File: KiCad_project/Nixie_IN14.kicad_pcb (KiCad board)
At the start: 2 copper layers, 455.7 x 86.7 mm, 62 parts, among them J1 Conn_01x10_Pin, J2 Conn_01x07_Pin, J3 Conn_01x07_Pin, J4 Conn_01x10_Pin, J5 Conn_01x07_Pin, J6 Conn_01x07_Pin, J7 USB_C_Receptacle_PowerOnly_6P, Q1 IRF540N, Q2 MMBTA42, U1 BME280_module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

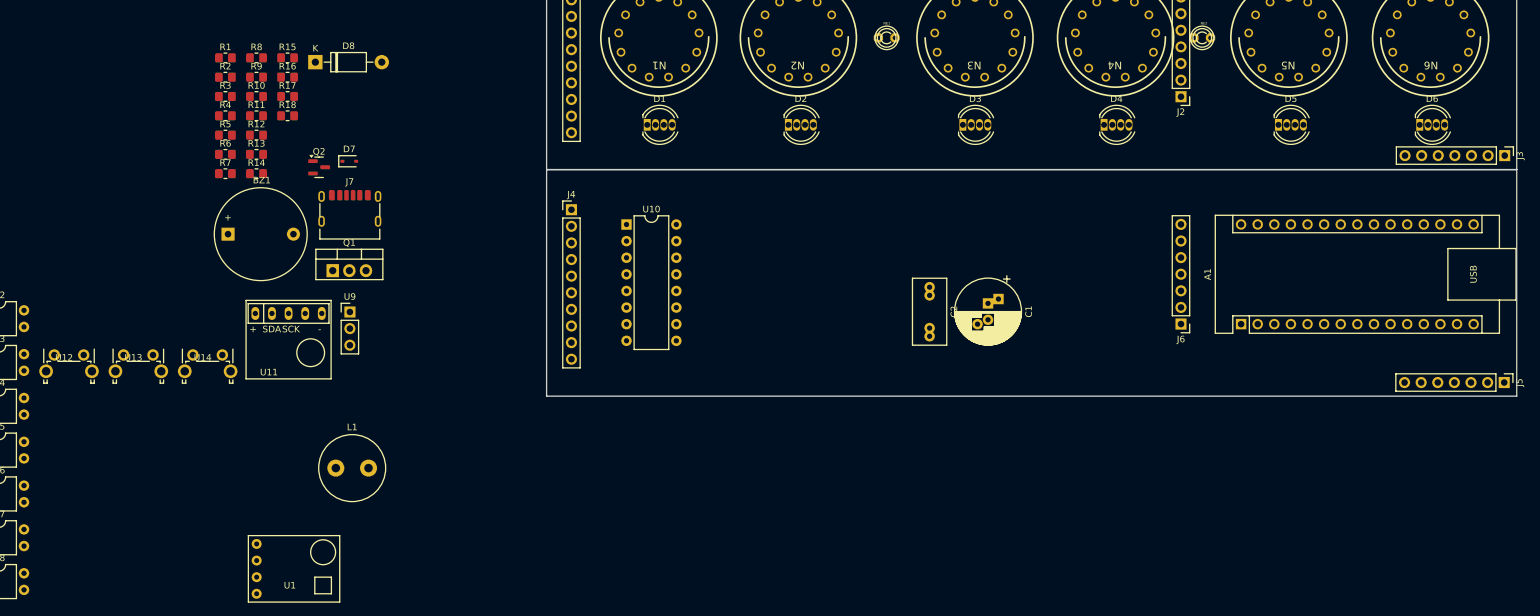
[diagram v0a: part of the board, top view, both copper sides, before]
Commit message: added missed power capacitors fixed some resistor values continue placing elements on the PCB
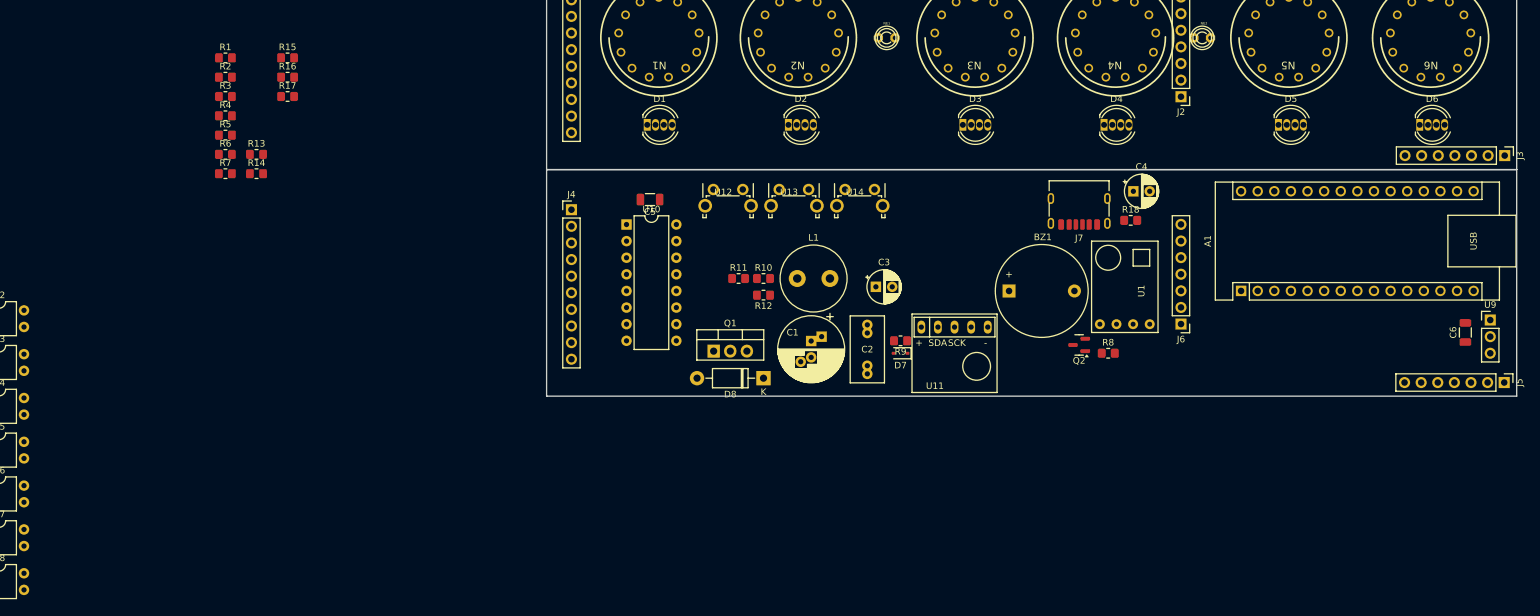
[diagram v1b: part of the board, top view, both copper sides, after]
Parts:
- added C3: 470uF x 6.3V, Capacitor_THT:CP_Radial_D5.0mm_P2.50mm, F.Cu at (194.3, -51.4)
- added C4: 470uF x 6.3V, Capacitor_THT:CP_Radial_D5.0mm_P2.50mm, F.Cu at (233.7, -66.0)
- added C5: 0.1uF, Capacitor_SMD:C_1206_3216Metric, F.Cu at (159.8, -64.8)
- added C6: 0.1uF, Capacitor_SMD:C_1206_3216Metric, F.Cu at (284.5, -44.5)
- moved U9 174.4 mm to (288.3, -46.4)
- moved R8 137.8 mm to (229.9, -41.3)
- moved U1 132.6 mm to (227.3, -44.5), turned to 90 degrees
- moved R18 129.9 mm to (233.3, -61.6)
- moved BZ1 119.7 mm to (214.7, -50.8)
- moved Q2 119.3 mm to (225.4, -42.5), turned to 180 degrees
- moved J7 111.5 mm to (225.4, -64.1), turned to 180 degrees
- moved R9 106.4 mm to (198.1, -43.2), turned to 180 degrees
- moved U12 103.9 mm to (171.0, -65.4)
- moved U13 103.4 mm to (181.1, -65.4)
- moved U14 102.9 mm to (191.1, -65.4)
- moved U11 101.8 mm to (206.4, -45.3)
- moved D7 89.3 mm to (198.1, -41.3), turned to 180 degrees
- moved D8 83.8 mm to (177.2, -37.5), turned to 180 degrees
- moved R10 82.4 mm to (177.2, -52.7)
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
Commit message: continue placing components
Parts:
- R10: value 100 -> 680k
- R11: value 100 -> 10k
- R8: value 5.1k -> 1k
- moved U3 224.3 mm to (280.7, -48.1), turned to -90 degrees
- moved U4 218.8 mm to (274.9, -48.1), turned to -90 degrees
- moved U5 213.3 mm to (268.8, -48.1), turned to -90 degrees
- moved U6 208.0 mm to (262.7, -48.0), turned to -90 degrees
- moved U2 200.2 mm to (256.7, -48.0), turned to -90 degrees
- moved U8 180.4 mm to (228.0, -63.6)
- moved U7 176.4 mm to (227.5, -57.7)
- moved R13 159.3 mm to (255.3, -37.6)
- moved R2 153.7 mm to (248.3, -73.6), turned to 180 degrees
- moved R14 153.5 mm to (250.7, -41.3), turned to 90 degrees
- moved R16 145.2 mm to (244.9, -46.8), turned to 180 degrees
- moved R17 145.0 mm to (244.9, -44.8), turned to 180 degrees
- moved R15 144.2 mm to (244.6, -52.6), turned to 90 degrees
- moved R7 129.5 mm to (221.8, -43.0), turned to 180 degrees
- moved R3 120.0 mm to (207.8, -40.0), turned to 90 degrees
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
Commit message: optimized placement for tracing added labels on schematic added capacitor for button
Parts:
- removed R1, R2: 330k, Resistor_SMD:R_0805_2012Metric_Pad1.20x1.40mm_HandSolder
- added C7: 0.1uF, Capacitor_SMD:C_1206_3216Metric, F.Cu at (132.4, 88.2)
- D8: footprint Diode_THT:D_DO-41_SOD81_P10.16mm_Horizontal -> Diode_THT:D_DO-41_SOD81_P7.62mm_Horizontal
- moved U4 219.6 mm to (123.2, 110.7)
- moved J1 216.4 mm to (22.5, 78.6), turned to 180 degrees
- moved J4 216.4 mm to (22.5, 113.2), turned to 180 degrees
- moved U3 211.5 mm to (140.7, 110.4)
- moved U5 211.3 mm to (129.2, 110.5)
- moved J2 210.8 mm to (77.3, 52.3), turned to 90 degrees
- moved J6 210.8 mm to (77.3, 87.1), turned to 90 degrees
- moved U10 209.3 mm to (34.3, 113.2), turned to 180 degrees
- moved U9 206.0 mm to (160.5, 113.4), turned to 90 degrees
- moved R16 203.4 mm to (107.5, 103.2), turned to 90 degrees
- moved Q1 202.3 mm to (39.0, 116.4)
- moved A1 202.0 mm to (125.3, 107.5)
- moved U7 201.5 mm to (116.9, 110.7), turned to -90 degrees
- moved U12 200.6 mm to (42.4, 88.5)
- moved U13 200.6 mm to (52.5, 88.5)
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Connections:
- net Net-(A1-A0) renamed A2_DECR
- net Net-(A1-A1) renamed A1_DECR
- net Net-(A1-A2) renamed A3_DECR
- net Net-(A1-A3) renamed A0_DECR
- net Net-(A1-A4) renamed SDA
- net Net-(A1-A5) renamed SCL
- net Net-(D1-BA) renamed LED_R_top
- net Net-(D1-GA) renamed LED_G_top
- net Net-(J2-Pin_3) renamed A1_top
- net Net-(J2-Pin_4) renamed A2_top
- net Net-(J2-Pin_5) renamed A3_top
- net Net-(J2-Pin_6) renamed A4_top
- net Net-(J3-Pin_6) renamed A5_top
- net Net-(J3-Pin_7) renamed A6_top
- net Net-(J4-Pin_1) renamed 8
- net Net-(J4-Pin_10) renamed 3
- net Net-(J4-Pin_2) renamed 9
- net Net-(J4-Pin_3) renamed 0
- net Net-(J4-Pin_4) renamed 1
- net Net-(J4-Pin_5) renamed 5
- net Net-(J4-Pin_6) renamed 2
- net Net-(J4-Pin_7) renamed 4
- net Net-(J4-Pin_8) renamed 6
- net Net-(J4-Pin_9) renamed 7
- A1 pad 26: Net-(A1-A7) -> Button
- D1 pad 4: Net-(D1-RA) -> LED_B_top
- D2 pad 4: Net-(D1-RA) -> LED_B_top
- D3 pad 4: Net-(D1-RA) -> LED_B_top
- D4 pad 4: Net-(D1-RA) -> LED_B_top
- D5 pad 4: Net-(D1-RA) -> LED_B_top
- D6 pad 4: Net-(D1-RA) -> LED_B_top
- J2 pad 2: Net-(J2-Pin_2) -> SEC_1_top
- J2 pad 7: unconnected-(J2-Pin_7-Pad7) -> LED_B_top
- J3 pad 4: Net-(D1-RA) -> LED_B_top
- J3 pad 5: Net-(J3-Pin_5) -> SEC_2_top
- NE1 pad 2: Net-(NE1-Pad2) -> SEC_1_top
- NE2 pad 2: Net-(NE2-Pad2) -> SEC_2_top
- R4 pad 1: Net-(A1-A7) -> BUTTON
- R5 pad 1: Net-(A1-A7) -> BUTTON
- U12 pad 1: Net-(A1-A7) -> BUTTON
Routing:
- net 3: track 0.00 -> 0.55 mm
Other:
- board size 455.7 x 86.7 mm -> 319.8 x 69.7 mm

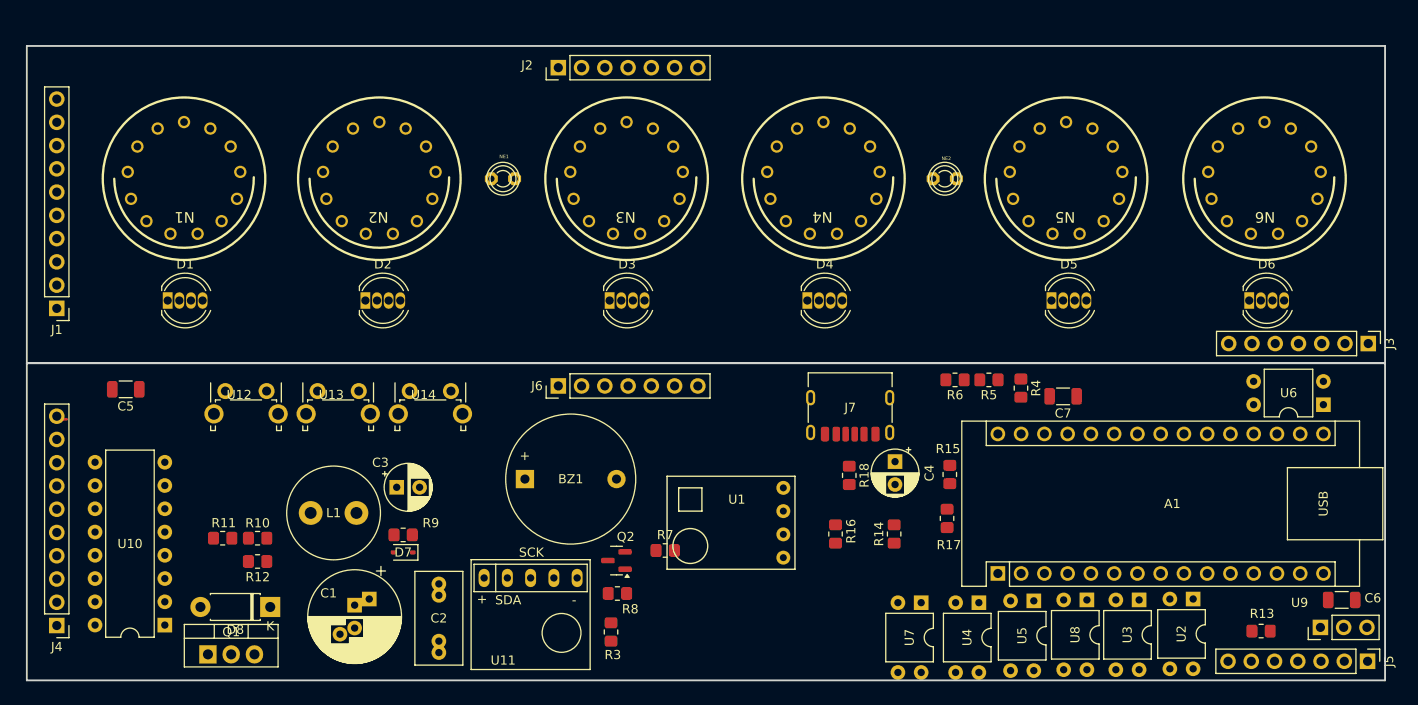
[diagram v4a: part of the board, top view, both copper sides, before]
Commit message: updated placement started routing
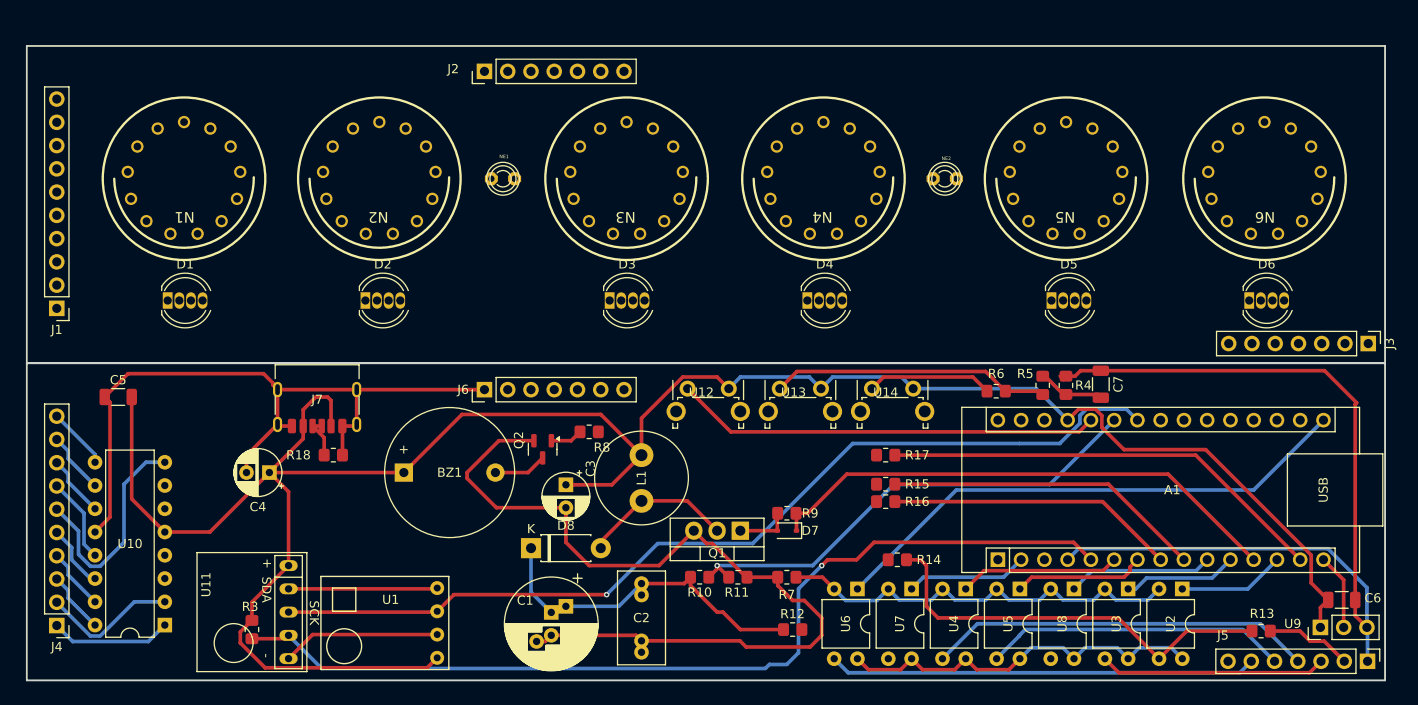
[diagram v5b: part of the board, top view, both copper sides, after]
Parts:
- moved C4 68.3 mm to (45.7, 96.5), turned to 180 degrees
- moved Q1 59.7 mm to (97.2, 102.9), turned to 180 degrees
- moved R12 58.9 mm to (102.9, 113.7), turned to 0 degrees
- moved J7 58.2 mm to (50.9, 88.3)
- moved R11 56.4 mm to (96.9, 108.0), turned to 180 degrees
- moved R18 56.4 mm to (52.7, 94.6), turned to 0 degrees
- moved U6 54.7 mm to (109.9, 109.2), turned to -90 degrees
- moved U13 50.5 mm to (103.0, 88.3)
- moved U14 50.5 mm to (113.0, 88.3)
- moved U12 50.5 mm to (92.9, 88.3)
- moved R10 48.5 mm to (92.7, 108.0), turned to 180 degrees
- moved D7 42.0 mm to (102.2, 102.9)
- moved R9 42.0 mm to (102.2, 101.0)
- moved U1 39.4 mm to (65.3, 118.0)
- moved R3 39.2 mm to (43.8, 113.7), turned to -90 degrees
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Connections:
- A1 pad 26: Button -> Controls
- C7 pad 1: BUTTON -> Controls
- D1 pad 2: GNDREF -> GND
- D2 pad 2: GNDREF -> GND
- D3 pad 2: GNDREF -> GND
- D4 pad 2: GNDREF -> GND
- D5 pad 2: GNDREF -> GND
- D6 pad 2: GNDREF -> GND
- J2 pad 1: GNDREF -> GND
- J2 pad 7: LED_B_top -> LED_B_top_NC
- J3 pad 1: GNDREF -> GND
- J5 pad 7: LED_B -> LED_B_NCC
- NE1 pad 1: GNDREF -> GND
- NE2 pad 1: GNDREF -> GND
- R4 pad 1: BUTTON -> Controls
- R5 pad 1: BUTTON -> Controls
- U12 pad 1: BUTTON -> Controls
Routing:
- net GNDREF: track 0.00 -> 293.9 mm
- net +5V: track 0.00 -> 244.7 mm
- net SQW: track 0.00 -> 103.9 mm, vias 0 -> 1
- net SCL: track 0.00 -> 102.9 mm, vias 0 -> 1
- net A4_CONTROL: track 0.00 -> 58.5 mm
- net PWM_PWR: track 0.00 -> 57.6 mm
- net Controls: track 0.00 -> 53.9 mm
- net CHECK_PWR: track 0.00 -> 53.4 mm, vias 0 -> 1
- net Net-(A1-D11): track 0.00 -> 49.0 mm
- net A4: track 0.00 -> 46.7 mm
- net Net-(R7-Pad1): track 0.00 -> 46.2 mm
- net Net-(R13-Pad1): track 0.00 -> 46.1 mm
- net A2: track 0.00 -> 42.1 mm
- net HIGH_VOLTAGE: track 0.00 -> 41.4 mm
- net Net-(D8-K): track 0.00 -> 35.9 mm
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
